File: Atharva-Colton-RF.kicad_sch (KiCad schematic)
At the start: 28 parts

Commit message: fixed balun logic for rx and tx
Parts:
- removed C? (x2): C, symbol Device:C
- removed L?: 0433BM15A0001, BALUM_FILTER(0805/SC70-6), symbol Atharva-Colton-RF-rescue:0433BM15A0001-0433BM15A0001
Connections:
- net GND: no longer U?.2 (RXp)
- net at C?.2: now also U?.4 (TX)
- net at T?.3: now also U?.2 (RXp); no longer U?.4 (TX)
- no-connect marks 11 -> 14

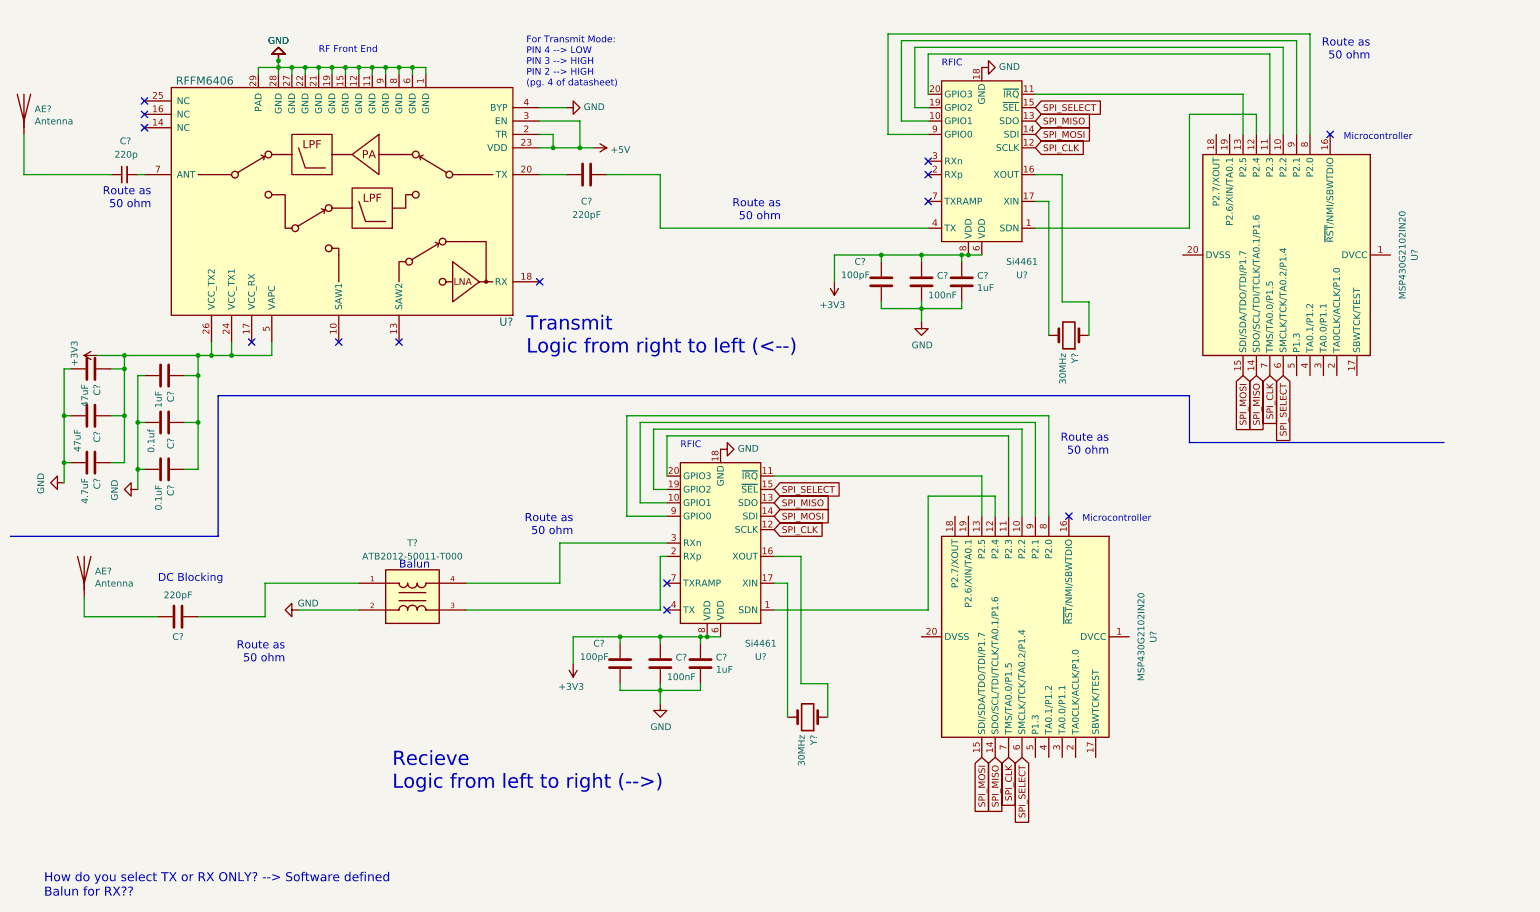
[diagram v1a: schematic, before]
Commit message: added connections to pins on uC that i did not know what to do with to a connector
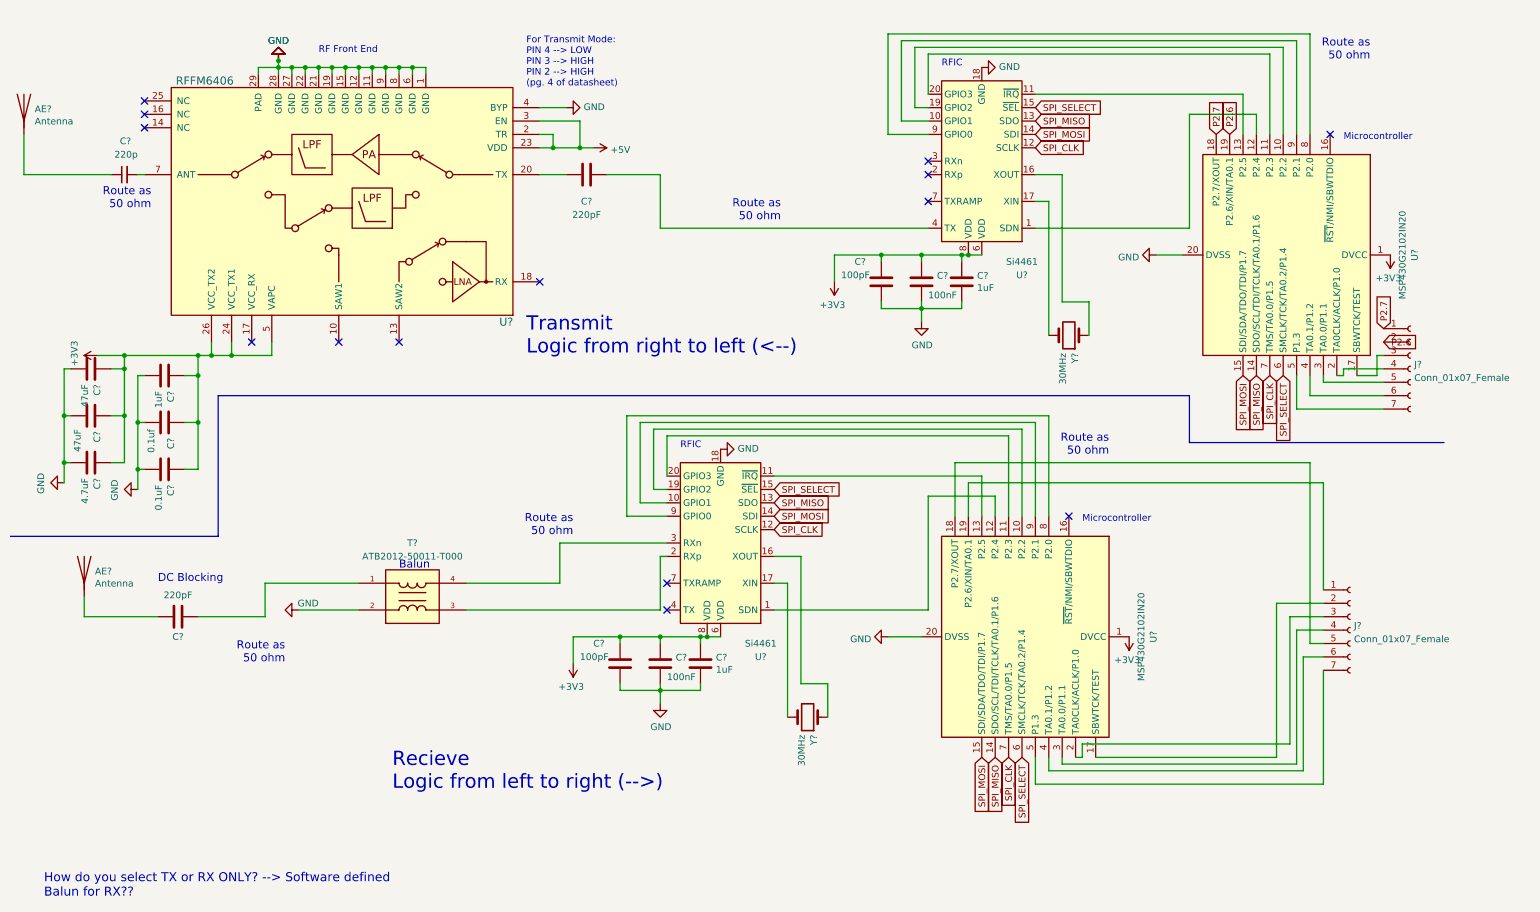
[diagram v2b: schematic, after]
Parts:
- added J? (x2): Conn_01x07_Female, symbol Connector:Conn_01x07_Female
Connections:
- net +3V3: now also U?.1 (DVCC), U?.1 (DVCC)
- net GND: now also U?.20 (DVSS), U?.20 (DVSS)
- net at U?.17 (SBWTCK/TEST): now also J?.2 (Pin_2)
- net at U?.18 (P2.7/XOUT): now also J?.5 (Pin_5)
- net at U?.19 (P2.6/XIN/TA0.1): now also J?.1 (Pin_1)
- net at U?.2 (TA0CLK/ACLK/P1.0): now also J?.3 (Pin_3)
- net at U?.3 (TA0.0/P1.1): now also J?.4 (Pin_4)
- net at U?.4 (TA0.1/P1.2): now also J?.6 (Pin_6) (x2)
- net at U?.5 (P1.3): now also J?.7 (Pin_7) (x2)
- net at U?.17 (SBWTCK/TEST): now also J?.3 (Pin_3)
- net P2.7: now reaches U?.18 (P2.7/XOUT)
- net P2.7: now also J?.1 (Pin_1)
- net P2.6: now reaches U?.19 (P2.6/XIN/TA0.1)
- net P2.6: now also J?.2 (Pin_2)
- net at U?.2 (TA0CLK/ACLK/P1.0): now also J?.4 (Pin_4)
- net at U?.3 (TA0.0/P1.1): now also J?.5 (Pin_5)

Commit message: pcb new init
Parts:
- C4: renamed from C?; footprint archive:C_0402_1005Metric -> (none)
- T1: renamed from T?; footprint XFMR_ATB2012-50011-T000 -> (none)
- gave numbers to parts that had none: 25
